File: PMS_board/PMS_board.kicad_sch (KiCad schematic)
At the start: 2 parts, among them K1 AZSR190

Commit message: Revert "Merge branch '2027_Rev1' of https://github.com/MissouriMRDT/PowerManagement_Hardware into 2027_Rev1"
This reverts commit 58e8d8a37d7e6e053a99adaceb0a0b64a7e4d5ac, reversing
changes made to 2dbcd4446407a5b00bde621a86c6c0759956a2a3.
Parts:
- removed ?: (no value), symbol Diode:1N53xxB
- removed K1: AZSR190, Relay_THT:Relay_SPST-NO_Fujitsu_FTR-LYAA005x_FormA_Vertical, symbol Relay:Relay_SPST-NO
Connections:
- no-connect marks 13 -> 15
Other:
- removed sheet D6
- removed sheet Voltage Sensing
- added sheet Battery Management (BatteryManagement.kicad_sch)
- note added: "Temporarily put no connects to make ERC shut up"

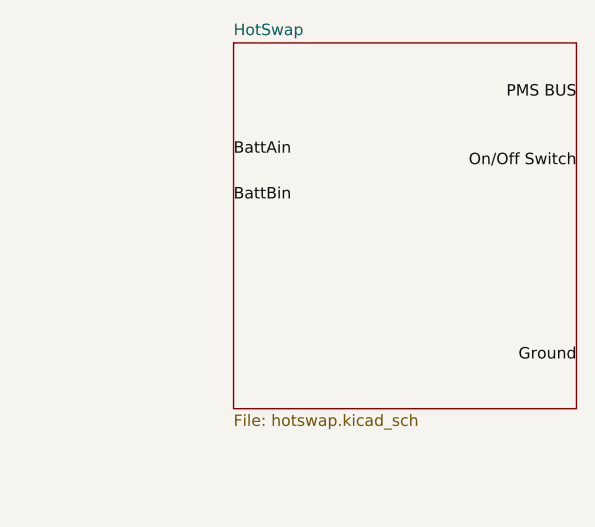
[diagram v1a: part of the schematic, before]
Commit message: Revert "Reapply "progress made :)""
This reverts commit d1e2932f9c3cdbb21c2c39973e18eebc9d543e4e.
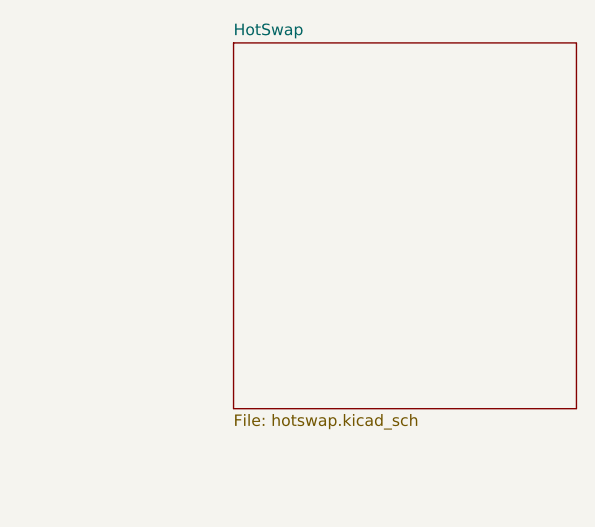
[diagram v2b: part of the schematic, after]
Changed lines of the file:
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@@
 		(at 73.66 72.39)
-	)
-	(label "BattAin"
-		(at 134.62 40.64 0)
-		(effects
-			(font
-				(size 1.27 1.27)
-			)
-			(justify left bottom)
-		)
-	)
-	(label "BattBin"
-		(at 134.62 45.72 0)
-		(effects
-			(font
-				(size 1.27 1.27)
-			)
-			(justify left bottom)
-		)
-	)
-	(label "Ground"
-		(at 172.72 63.5 180)
-		(effects
-			(font
-				(size 1.27 1.27)
-			)
-			(justify right bottom)
-		)
-	)
-	(label "On{slash}Off Switch"
-		(at 172.72 41.91 180)
-		(effects
-			(font
-				(size 1.27 1.27)
-			)
-			(justify right bottom)
-		)
-	)
-	(label "PMS BUS"
-		(at 172.72 34.29 180)
-		(effects
-			(font
-				(size 1.27 1.27)
-			)
-			(justify right bottom)
-		)
 	)
 	(sheet

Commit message: Nuked L9962 :(
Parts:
- added D6: 1N5359B, Diode_THT:D_DO-201_P15.24mm_Horizontal, symbol Diode:1N53xxB
- added K1: AZSR190, Relay_THT:Relay_SPST-NO_Fujitsu_FTR-LYAA005x_FormA_Vertical, symbol Relay:Relay_SPST-NO
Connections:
- new net +24V: K1.14
- new net ESTOP: D6.1 (K), K1.A1
- new net PACK+: K1.13
- new net PACK-: D6.2 (A), K1.A2
- no-connect marks 15 -> 0
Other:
- removed sheet Battery Management
- note removed: "Temporarily put no connects to make ERC shut up"

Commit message: Voltage Sensing YIPPEEEEE
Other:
- added sheet Voltage Sensing (VoltageSensing.kicad_sch)
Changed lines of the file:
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@@
 		)
 	)
-	(hierarchical_label "ESTOP"
-		(shape input)
-		(at 53.34 152.4 90)
+	(label "ESTOP"
+		(at 53.34 152.4 0)
 		(effects
 			(font
 				(size 1.27 1.27)
 			)
-			(justify left)
+			(justify left bottom)
 		)
 	)
@@
 				)
 			)
+		)
+	)
+	(sheet
+		(at 31.75 33.02)
+		(size 39.37 27.94)
+		(exclude_from_sim no)
+		(in_bom yes)
+		(on_board yes)
+		(dnp no)
+		(fields_autoplaced yes)
+		(stroke
+			(width 0.1524)
+			(type solid)
+		)
+		(fill
+			(color 0 0 0 0)
+		)
+		(property "Sheetname" "Voltage Sensing"
+			(at 31.75 32.3084 0)
+			(show_name no)
+			(do_not_autoplace no)
+			(effects
+				(font
+					(size 1.27 1.27)
+				)
+				(justify left bottom)
+			)
+		)
+		(property "Sheetfile" "VoltageSensing.kicad_sch"
+			(at 31.75 61.5446 0)
+			(show_name no)
+			(do_not_autoplace no)
+			(effects
+				(font
+					(size 1.27 1.27)
+				)
+				(justify left top)
+			)
+		)
+		(pin "CELL1" input
+			(at 31.75 41.91 180)
+			(effects
+				(font
+					(size 1.27 1.27)
+				)
+				(justify left)
+			)
+		)
+		(pin "CELL2" input
+			(at 31.75 44.45 180)
+			(effects
+				(font
+					(size 1.27 1.27)
+				)
+				(justify left)
+			)
+		)
+		(pin "CELL3" input
+			(at 31.75 46.99 180)
+			(effects
+				(font
+					(size 1.27 1.27)
+				)
+				(justify left)
+			)
+		)
+		(pin "CELL4" input
+			(at 31.75 49.53 180)
+			(effects
+				(font
+					(size 1.27 1.27)
+				)
+				(justify left)
+			)
+		)
+		(pin "CELL5" input
+			(at 31.75 52.07 180)
+			(effects
+				(font
+					(size 1.27 1.27)
+				)
+				(justify left)
+			)
+		)
+		(pin "CELL6" input
+			(at 31.75 54.61 180)
+			(effects
+				(font
+					(size 1.27 1.27)
+				)
+				(justify left)
+			)
+		)
+		(pin "VSENSE1" input
+			(at 71.12 41.91 0)
+			(effects
+				(font
+					(size 1.27 1.27)
+				)
+				(justify right)
+			)
+		)
+		(pin "VSENSE2" input
+			(at 71.12 44.45 0)
+			(effects
+				(font
+					(size 1.27 1.27)
+				)
+				(justify right)
+			)
+		)
+		(pin "VSENSE3" input
+			(at 71.12 46.99 0)
+			(effects
+				(font
+					(size 1.27 1.27)
+				)
+				(justify right)
+			)
+		)
+		(pin "VSENSE4" input
+			(at 71.12 49.53 0)
+			(effects
+				(font
+					(size 1.27 1.27)
+				)
+				(justify right)
+			)
+		)
+		(pin "VSENSE5" input
+			(at 71.12 52.07 0)
+			(effects
+				(font
+					(size 1.27 1.27)
+				)
+				(justify right)
+			)
+		)
+		(pin "VSENSE6" input
+			(at 71.12 54.61 0)
+			(effects
+				(font
+					(size 1.27 1.27)
+				)
+				(justify right)
+			)
+		)
+		(instances
+			(project "PMS_board"
+				(path "/282246b0-e0d8-4997-b3ee-58bf10355d52"
+					(page "2")
+				)
+			)
